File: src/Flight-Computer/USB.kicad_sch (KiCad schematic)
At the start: 1 part

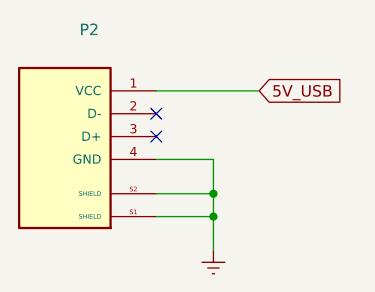
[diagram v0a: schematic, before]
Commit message: implemented crystal oscillator in schematic
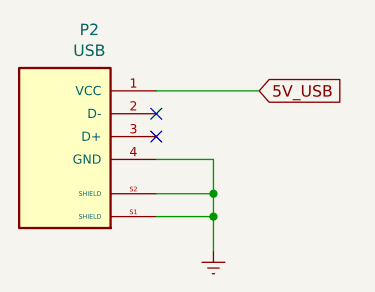
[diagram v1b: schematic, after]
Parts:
- P2: value (none) -> USB; footprint (none) -> Engine-Controller:USB-TypeB
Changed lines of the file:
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@@
       (effects (font (size 1.27 1.27)) hide)
     )
-    (property "Value" "" (id 1) (at 151.13 120.65 0)
+    (property "Value" "Earth" (id 1) (at 151.13 120.65 0)
       (effects (font (size 1.27 1.27)) hide)
     )
@@
     (in_bom yes) (on_board yes)
     (property "Reference" "P2" (id 0) (at 137.3378 92.2782 0))
-    (property "Value" "" (id 1) (at 137.3378 94.5896 0))
-    (property "Footprint" "" (id 2) (at 143.51 121.92 0)
+    (property "Value" "USB" (id 1) (at 137.3378 94.5896 0))
+    (property "Footprint" "Engine-Controller:USB-TypeB" (id 2) (at 143.51 121.92 0)
       (effects (font (size 1.27 1.27)) (justify left bottom) hide)
     )
